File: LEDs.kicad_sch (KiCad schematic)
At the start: 41 parts, among them Q2 NX6008NBKWX

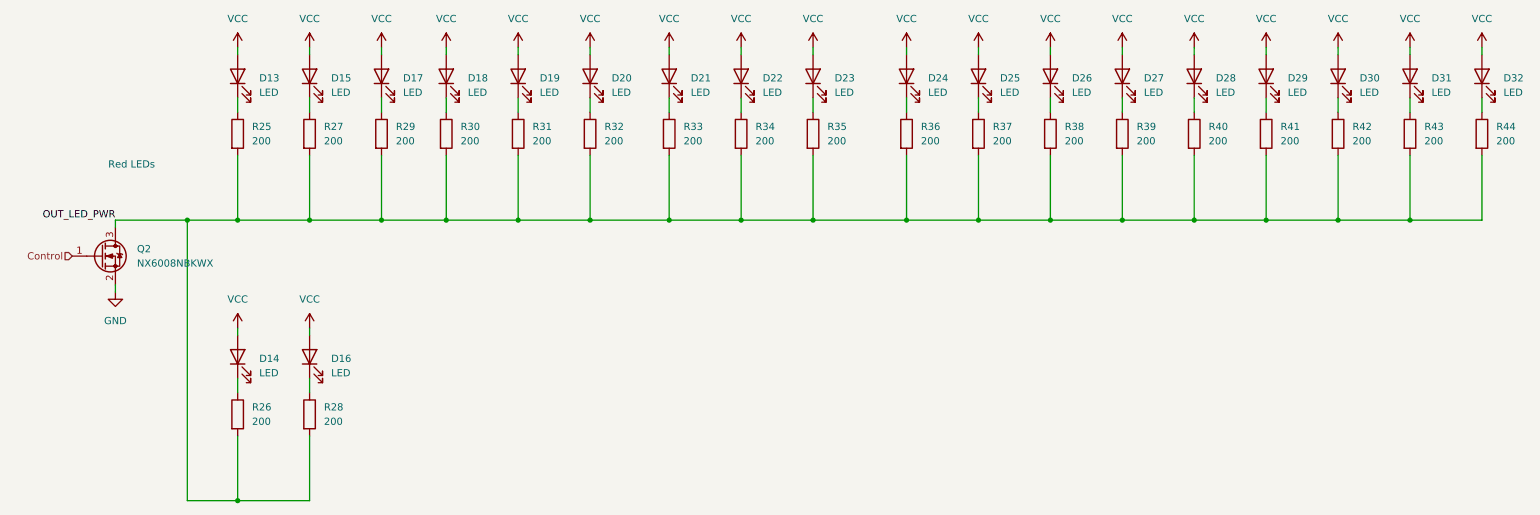
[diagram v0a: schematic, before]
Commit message: Add BoM and complete board
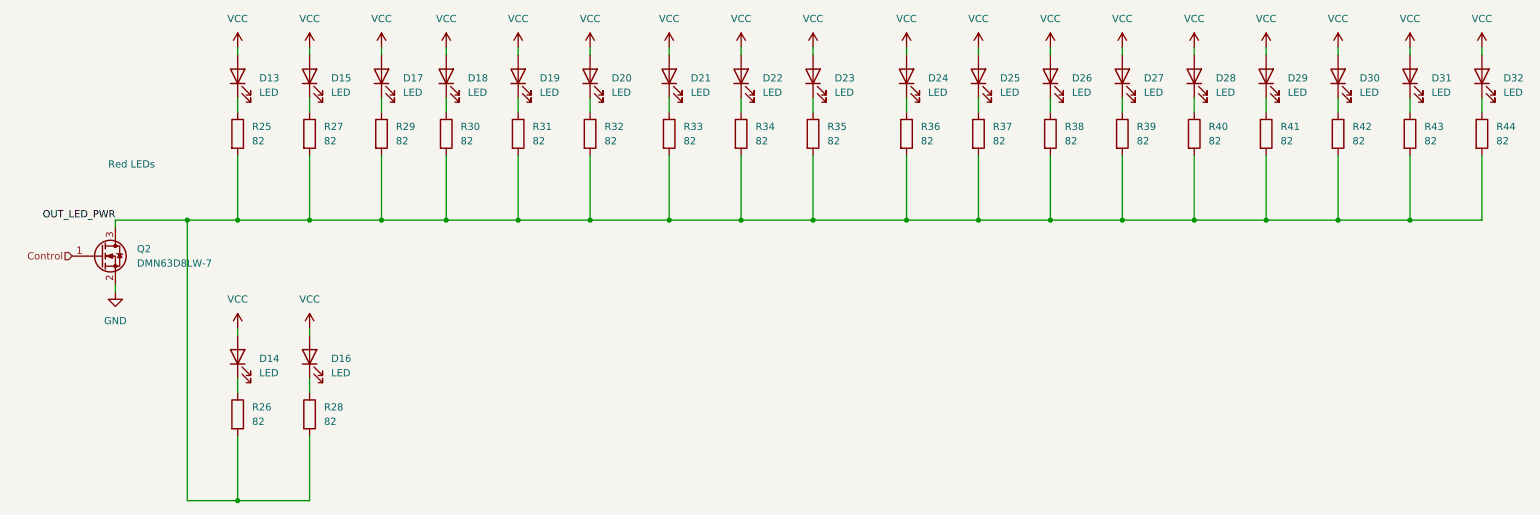
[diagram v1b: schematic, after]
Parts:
- Q2: value NX6008NBKWX -> DMN63D8LW-7
- R25, R26, R27, R28, R29, R30, R31, R32, R33, R34, R35, R36, R37, R38, R39, R40, R41, R42, R43, R44: value 200 -> 82
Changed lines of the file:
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@@
       (effects (font (size 1.27 1.27)) (justify left))
     )
-    (property "Value" "200" (id 1) (at 57.15 118.1099 0)
+    (property "Value" "82" (id 1) (at 57.15 118.1099 0)
       (effects (font (size 1.27 1.27)) (justify left))
     )
@@
       (effects (font (size 1.27 1.27)) (justify left))
     )
-    (property "Value" "200" (id 1) (at 213.36 68.5799 0)
+    (property "Value" "82" (id 1) (at 213.36 68.5799 0)
       (effects (font (size 1.27 1.27)) (justify left))
     )
@@
       (effects (font (size 1.27 1.27)) (justify left))
     )
-    (property "Value" "200" (id 1) (at 251.46 68.5799 0)
+    (property "Value" "82" (id 1) (at 251.46 68.5799 0)
       (effects (font (size 1.27 1.27)) (justify left))
     )
@@
       (effects (font (size 1.27 1.27)) (justify left))
     )
-    (property "Value" "200" (id 1) (at 93.98 68.5799 0)
+    (property "Value" "82" (id 1) (at 93.98 68.5799 0)
       (effects (font (size 1.27 1.27)) (justify left))
     )
@@
       (effects (font (size 1.27 1.27)) (justify left))
     )
-    (property "Value" "NX6008NBKWX" (id 1) (at 36.83 90.1699 0)
+    (property "Value" "DMN63D8LW-7" (id 1) (at 36.83 90.1699 0)
       (effects (font (size 1.27 1.27)) (justify left))
     )
@@
       (effects (font (size 1.27 1.27)) (justify left))
     )
-    (property "Value" "200" (id 1) (at 175.26 68.5799 0)
+    (property "Value" "82" (id 1) (at 175.26 68.5799 0)
       (effects (font (size 1.27 1.27)) (justify left))
     )
@@
       (effects (font (size 1.27 1.27)) (justify left))
     )
-    (property "Value" "200" (id 1) (at 276.86 68.5799 0)
+    (property "Value" "82" (id 1) (at 276.86 68.5799 0)
       (effects (font (size 1.27 1.27)) (justify left))
     )
@@
       (effects (font (size 1.27 1.27)) (justify left))
     )
-    (property "Value" "200" (id 1) (at 238.76 68.5799 0)
+    (property "Value" "82" (id 1) (at 238.76 68.5799 0)
       (effects (font (size 1.27 1.27)) (justify left))
     )
@@
       (effects (font (size 1.27 1.27)) (justify left))
     )
-    (property "Value" "200" (id 1) (at 226.06 68.5799 0)
+    (property "Value" "82" (id 1) (at 226.06 68.5799 0)
       (effects (font (size 1.27 1.27)) (justify left))
     )
@@
       (effects (font (size 1.27 1.27)) (justify left))
     )
-    (property "Value" "200" (id 1) (at 146.05 68.5799 0)
+    (property "Value" "82" (id 1) (at 146.05 68.5799 0)
       (effects (font (size 1.27 1.27)) (justify left))
     )
@@
       (effects (font (size 1.27 1.27)) (justify left))
     )
-    (property "Value" "200" (id 1) (at 69.85 68.5799 0)
+    (property "Value" "82" (id 1) (at 69.85 68.5799 0)
       (effects (font (size 1.27 1.27)) (justify left))
     )
@@
       (effects (font (size 1.27 1.27)) (justify left))
     )
-    (property "Value" "200" (id 1) (at 133.35 68.5799 0)
+    (property "Value" "82" (id 1) (at 133.35 68.5799 0)
       (effects (font (size 1.27 1.27)) (justify left))
     )
@@
       (effects (font (size 1.27 1.27)) (justify left))
     )
-    (property "Value" "200" (id 1) (at 69.85 118.1099 0)
+    (property "Value" "82" (id 1) (at 69.85 118.1099 0)
       (effects (font (size 1.27 1.27)) (justify left))
     )
@@
       (effects (font (size 1.27 1.27)) (justify left))
     )
-    (property "Value" "200" (id 1) (at 200.66 68.5799 0)
+    (property "Value" "82" (id 1) (at 200.66 68.5799 0)
       (effects (font (size 1.27 1.27)) (justify left))
     )
@@
       (effects (font (size 1.27 1.27)) (justify left))
     )
-    (property "Value" "200" (id 1) (at 187.96 68.5799 0)
+    (property "Value" "82" (id 1) (at 187.96 68.5799 0)
       (effects (font (size 1.27 1.27)) (justify left))
     )
@@
       (effects (font (size 1.27 1.27)) (justify left))
     )
-    (property "Value" "200" (id 1) (at 57.15 68.5799 0)
+    (property "Value" "82" (id 1) (at 57.15 68.5799 0)
       (effects (font (size 1.27 1.27)) (justify left))
     )
@@
       (effects (font (size 1.27 1.27)) (justify left))
     )
-    (property "Value" "200" (id 1) (at 264.16 68.5799 0)
+    (property "Value" "82" (id 1) (at 264.16 68.5799 0)
       (effects (font (size 1.27 1.27)) (justify left))
     )
@@
       (effects (font (size 1.27 1.27)) (justify left))
     )
-    (property "Value" "200" (id 1) (at 158.75 68.5799 0)
+    (property "Value" "82" (id 1) (at 158.75 68.5799 0)
       (effects (font (size 1.27 1.27)) (justify left))
     )
@@
       (effects (font (size 1.27 1.27)) (justify left))
     )
-    (property "Value" "200" (id 1) (at 82.55 68.5799 0)
+    (property "Value" "82" (id 1) (at 82.55 68.5799 0)
       (effects (font (size 1.27 1.27)) (justify left))
     )
@@
       (effects (font (size 1.27 1.27)) (justify left))
     )
-    (property "Value" "200" (id 1) (at 119.38 68.5799 0)
+    (property "Value" "82" (id 1) (at 119.38 68.5799 0)
       (effects (font (size 1.27 1.27)) (justify left))
     )
@@
       (effects (font (size 1.27 1.27)) (justify left))
     )
-    (property "Value" "200" (id 1) (at 106.68 68.5799 0)
-      (effects (font (size 1.27 1.27)) (justify left))
-    )
+    (property "Value" "82" (id 1) (at 106.68 68.5799 0)
+      (effects (font (size 1.27 1.27)) (justify left))
+    )
